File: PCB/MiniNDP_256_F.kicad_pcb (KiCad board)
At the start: 2 copper layers, 60 x 34 mm, 16 parts, among them J1 Conn_02x20_Odd_Even, U1 HC238, U2 HC4040, U3 HC573, U4 AS6C2008A_DIP32_SOP32

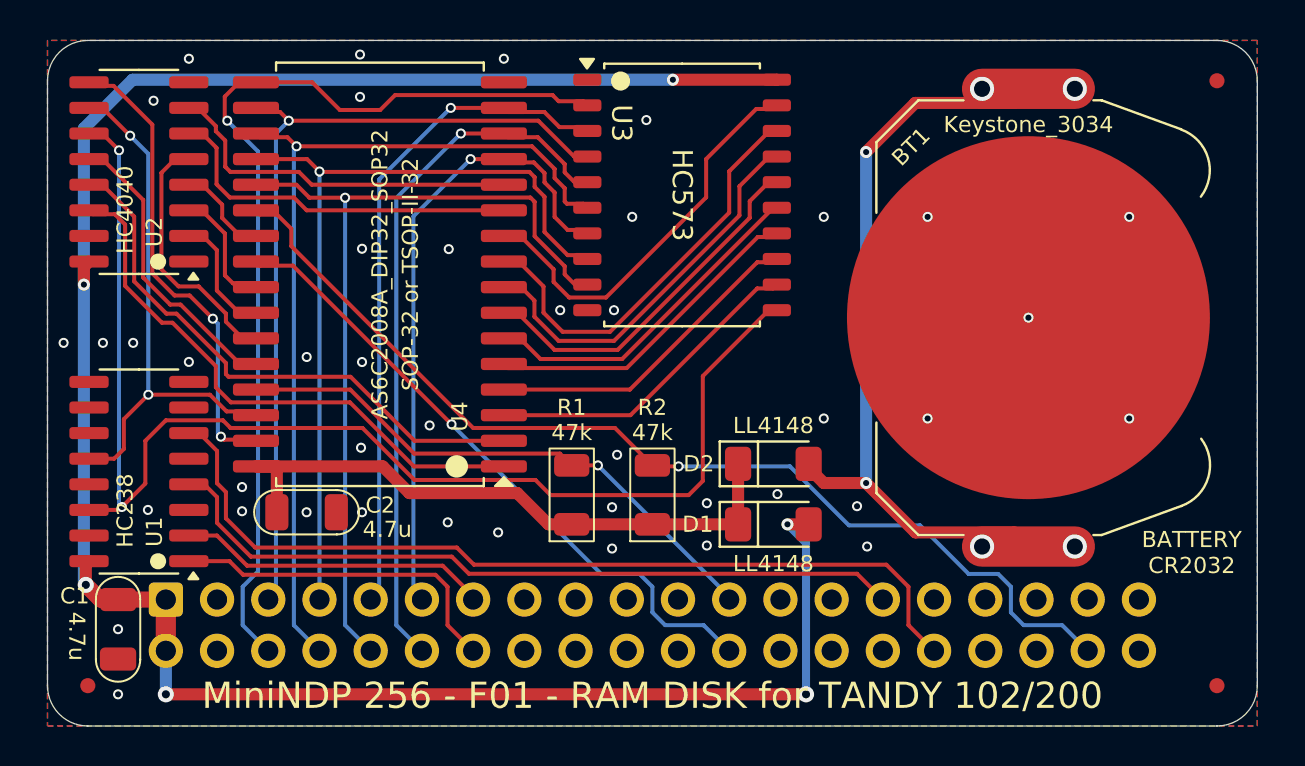
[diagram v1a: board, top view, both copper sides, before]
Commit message: 512-F re-add ramrst diode, both-F remove /WR pullup
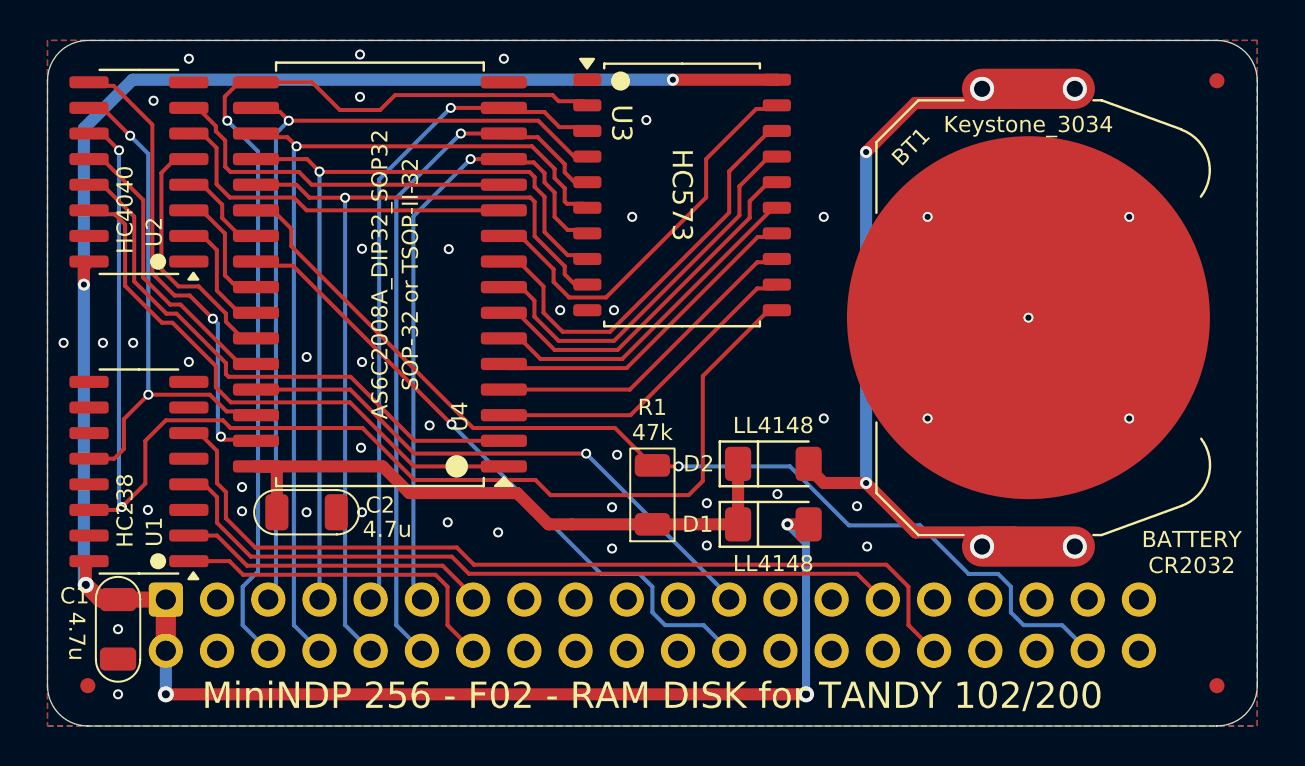
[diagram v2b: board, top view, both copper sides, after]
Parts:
- removed the R1 at (147.9, 108.6)
- renumbered R2 to R1

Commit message: easy boards add 47u cap, remove ramrst diode
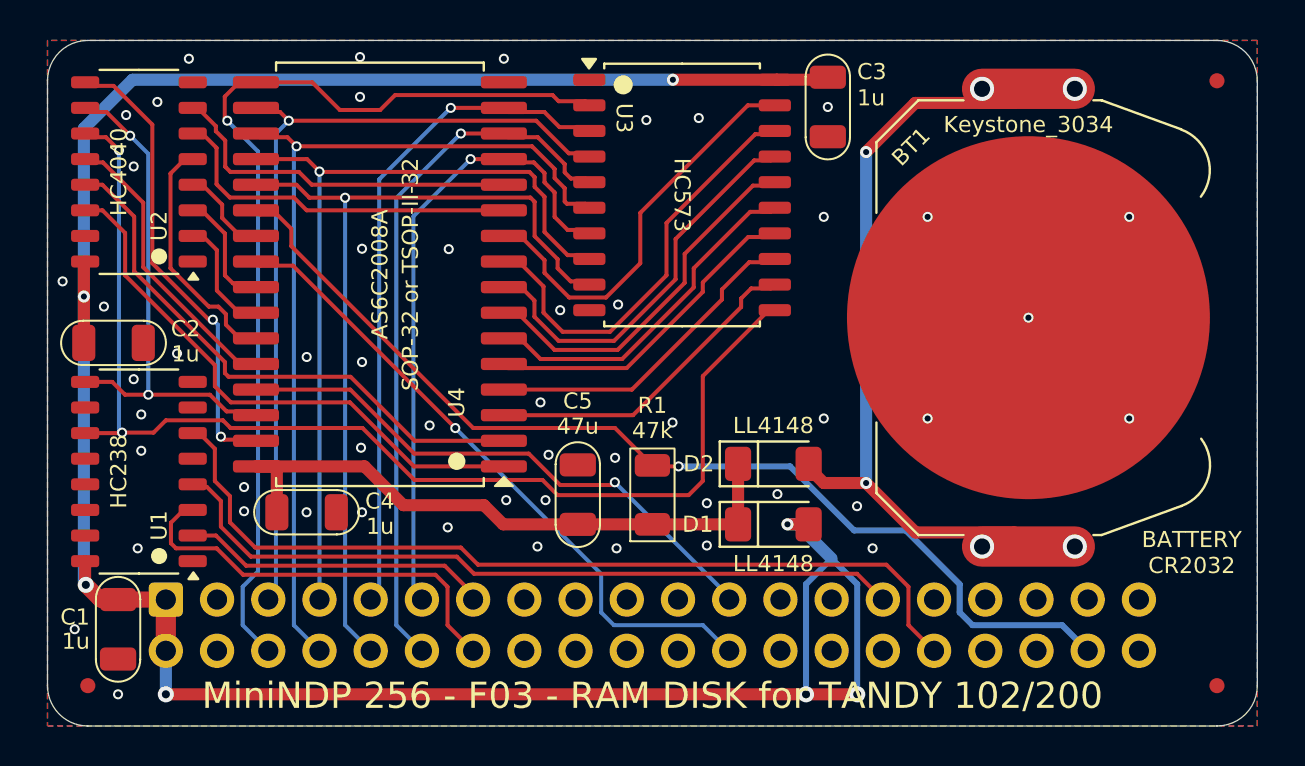
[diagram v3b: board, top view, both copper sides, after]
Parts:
- added C2: 1u, 000_LOCAL:C_1206, F.Cu at (125.2, 101.0)
- added C3: 1u, 000_LOCAL:C_1206, F.Cu at (160.7, 89.3)
- added C5: 47u, 000_LOCAL:C_1206, F.Cu at (148.2, 108.5)
- C1: value 4.7u -> 1u
- C4: renamed from C2; value 4.7u -> 1u
- U4: value AS6C2008A_DIP32_SOP32 -> AS6C2008A
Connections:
- U1 pad 1: /BUS_A8 -> GND
- U1 pad 11: unconnected-(U1-Y4-Pad11) -> /BLOCK
- U1 pad 12: /BYTE -> unconnected-(U1-Y3-Pad12)
- U1 pad 14: /BLOCK -> unconnected-(U1-Y1-Pad14)
- U1 pad 3: GND -> /BUS_A8
- U1 pad 9: unconnected-(U1-Y6-Pad9) -> /BYTE
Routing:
- net VBUS: track 111.1 -> 127.6 mm, vias 6 -> 7
- net /BLOCK: track 65.2 -> 58.9 mm
- net /BUS_A8: track 17.1 -> 20.7 mm
- net /BYTE: track 26.7 -> 25.2 mm
- net /A3: track 12.8 -> 12.1 mm
- net GND: vias 43 -> 52

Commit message: bundle code font
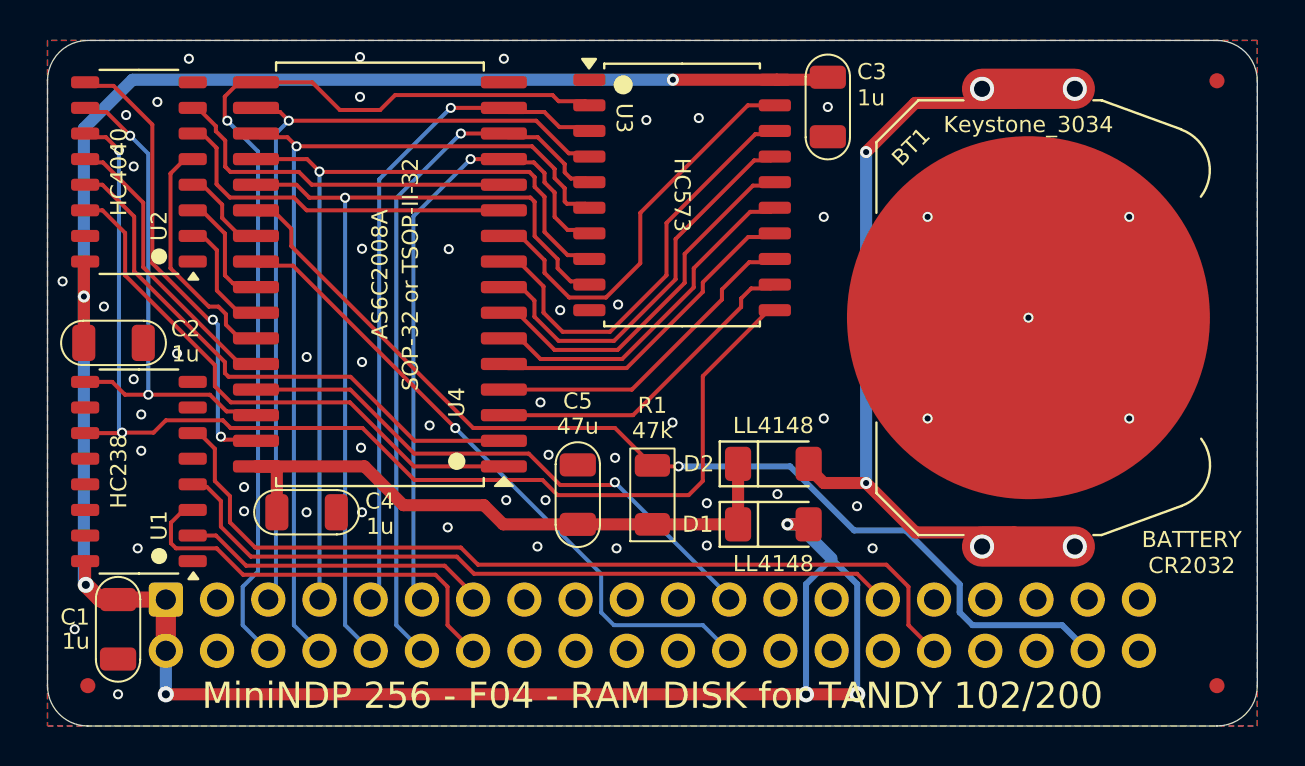
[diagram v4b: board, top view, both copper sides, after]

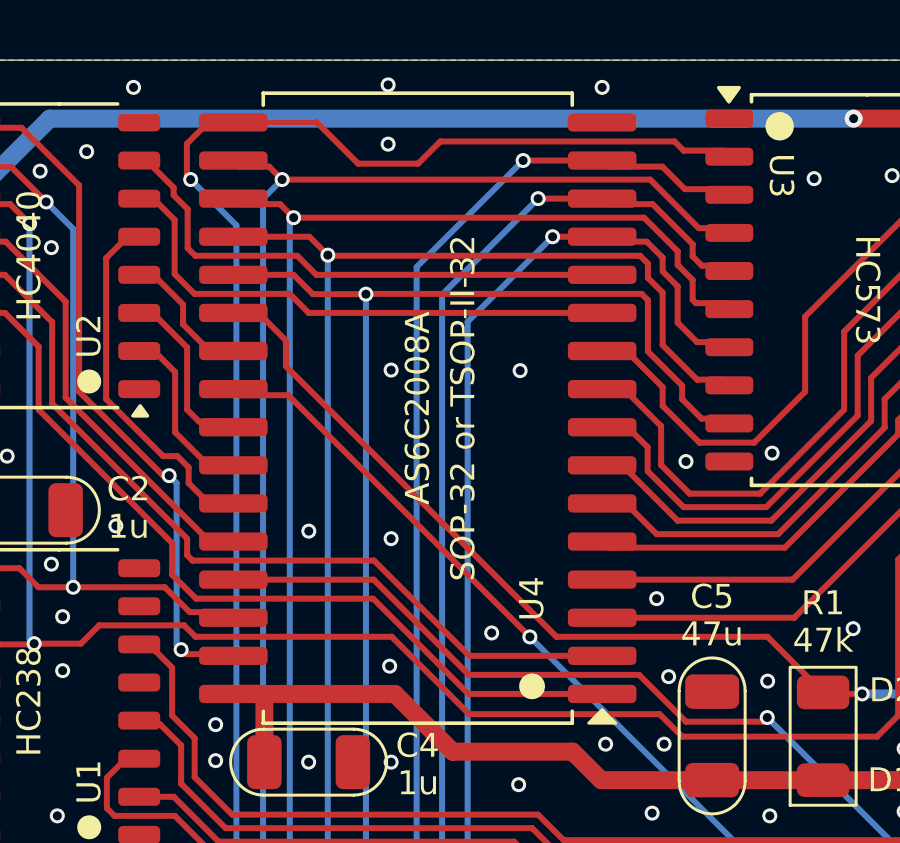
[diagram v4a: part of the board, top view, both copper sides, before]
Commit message: 256_F wrong sram part# on silkscreen
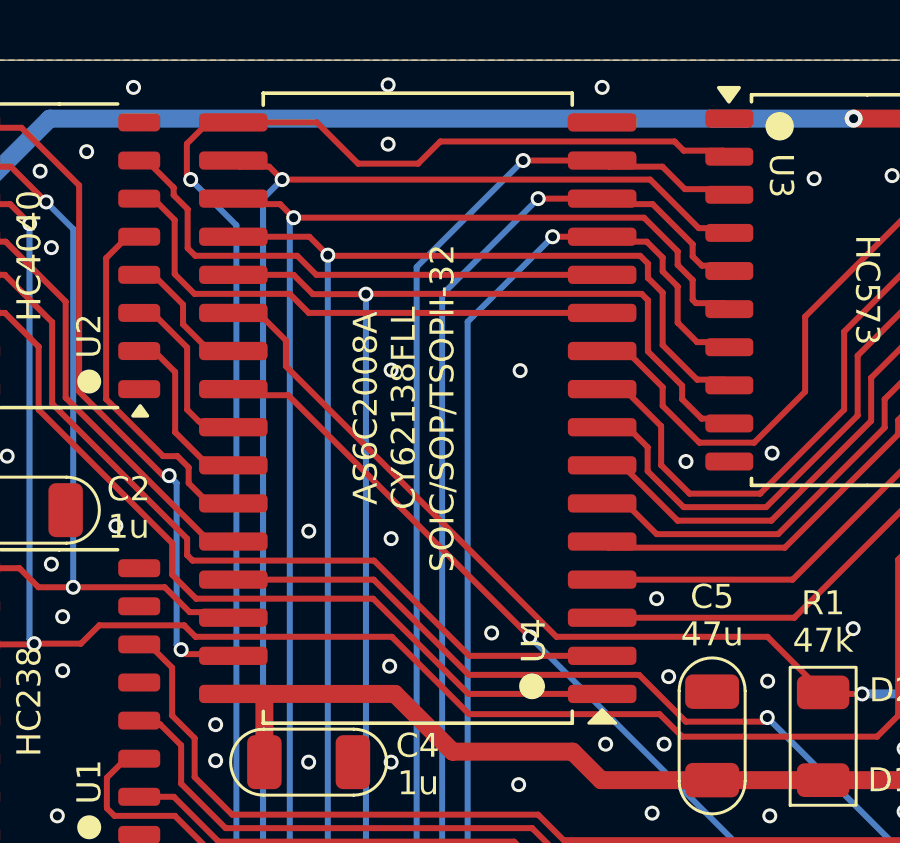
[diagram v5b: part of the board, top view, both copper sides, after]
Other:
- board text added: "CY62138FLL SOIC/SOP/TSOPII-32"
- board text added: "Use ENIG copper finish for gold battery terminal"
- board text removed: "SOP-32 or TSOP-II-32"
- board text removed: "Use ENIG copper finish for gold plated battery terminal"
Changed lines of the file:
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@@
 		(tags "TSOP-II 32")
 		(property "Reference" "U4"
-			(at -3.81 -7.099 90)
+			(at -3.8628 -8.499 90)
 			(unlocked yes)
 			(layer "F.SilkS")
@@
 		)
 		(property "Value" "AS6C2008A"
-			(at 0 0 90)
+			(at 1.7372 0 90)
 			(unlocked yes)
 			(layer "F.SilkS")
@@
 		)
 	)
-	(gr_text "SOP-32 or TSOP-II-32"
-		(at 139.95 97.625 90)
+	(gr_text "CY62138FLL\nSOIC/SOP/TSOPII-32"
+		(at 137.5 97.625 90)
 		(layer "F.SilkS")
 		(effects
@@
 				(thickness 0.1)
 			)
+			(justify top)
 		)
 	)
@@
 		)
 	)
-	(gr_text "Use ENIG copper finish\nfor gold plated battery terminal"
-		(at 170.6 84.025 0)
-		(layer "Dwgs.User")
+	(gr_text "Use ENIG copper finish\nfor gold battery terminal"
+		(at 170.6 85.025 0)
+		(layer "Eco1.User")
 		(effects
 			(font
@@
 				(thickness 0.15)
 			)
+			(justify bottom)
 		)
 	)

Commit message: 256_F back pic
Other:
- board text added: "Install the font in the font directory for the BASIC code."
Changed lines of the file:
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@@
+		)
+	)
+	(gr_text "Install the font in the font\ndirectory for the BASIC code."
+		(at 151.95 85.025 0)
+		(layer "Eco2.User")
+		(effects
+			(font
+				(size 1 1)
+				(thickness 0.15)
+			)
+			(justify bottom mirror)
 		)
 	)

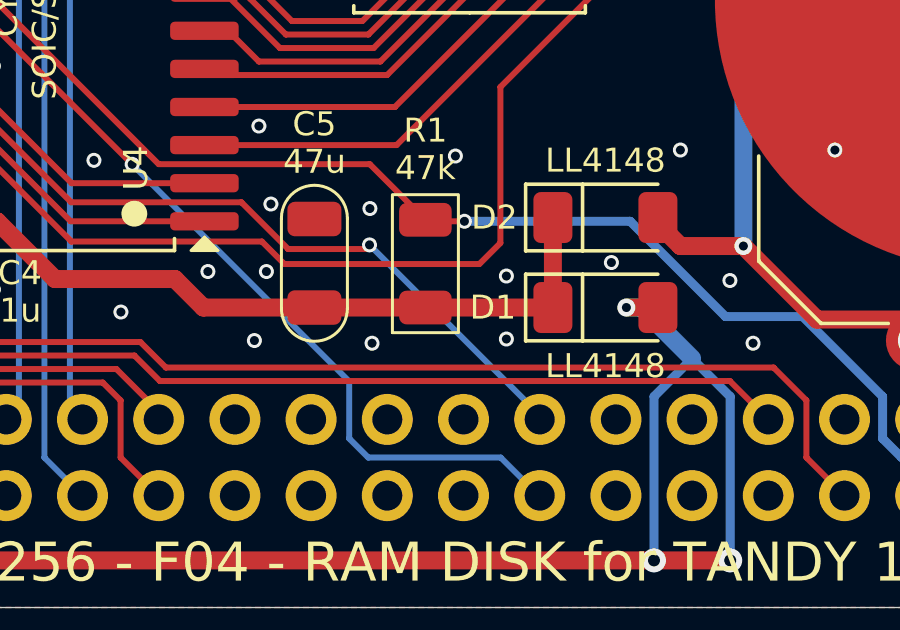
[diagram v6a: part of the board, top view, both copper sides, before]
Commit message: ez1m rear silkscreen programming reference
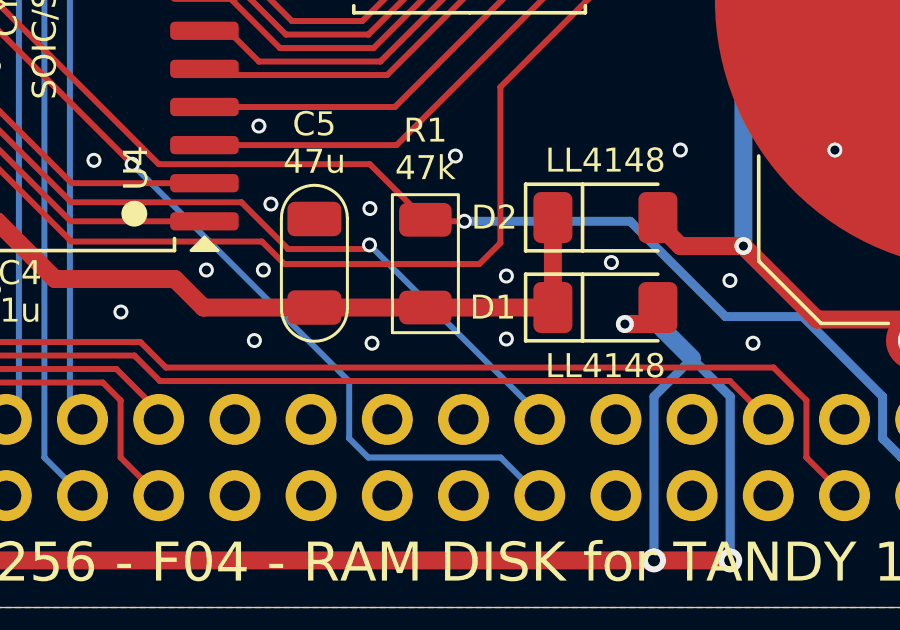
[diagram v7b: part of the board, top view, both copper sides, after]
